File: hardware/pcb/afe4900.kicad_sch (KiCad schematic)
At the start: 19 parts, among them U15 TPS61240YFFR, U16 SFH 7072, U6 AFE4900YZR

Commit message: Fix the review's datasheet errors without changing respiration or the GDTs.
Replace the MCP73831 with a BQ25170 so a flat cell still charges from USB, add the missing series protection and ESP32/CP2102 passives, and withdraw the claim that respiration still works with 51 kΩ in the loop.

Co-authored-by: Riyu-D1 <Riyu-D1@users.noreply.github.com>
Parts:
- R43, R45: value 10M -> 5.11M
- R44, R46: value 10M -> 100k
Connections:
- net +3V3: no longer R43.1, R45.1
- net AFE_INM: no longer R46.1
- net AFE_INP: no longer R44.1
- net AFE_N_AC: now also R46.1; no longer C57.1
- net AFE_P_AC: now also R44.1; no longer C56.1
- net GND: no longer R44.2, R46.2
- new net AFE_N_SER: C57.1, R46.2
- new net AFE_P_SER: C56.1, R44.2
- new net RLDOUT: R43.1, R45.1
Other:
- note added: "R44/R46 are 100k on the TPD side. R43/R45 bias from ADS RLDOUT, not a second RLD amp."
- note removed: "R9 holds RESETZ down until the expander drives it. R10 holds CLK low. AFE RLD_OUT is open."

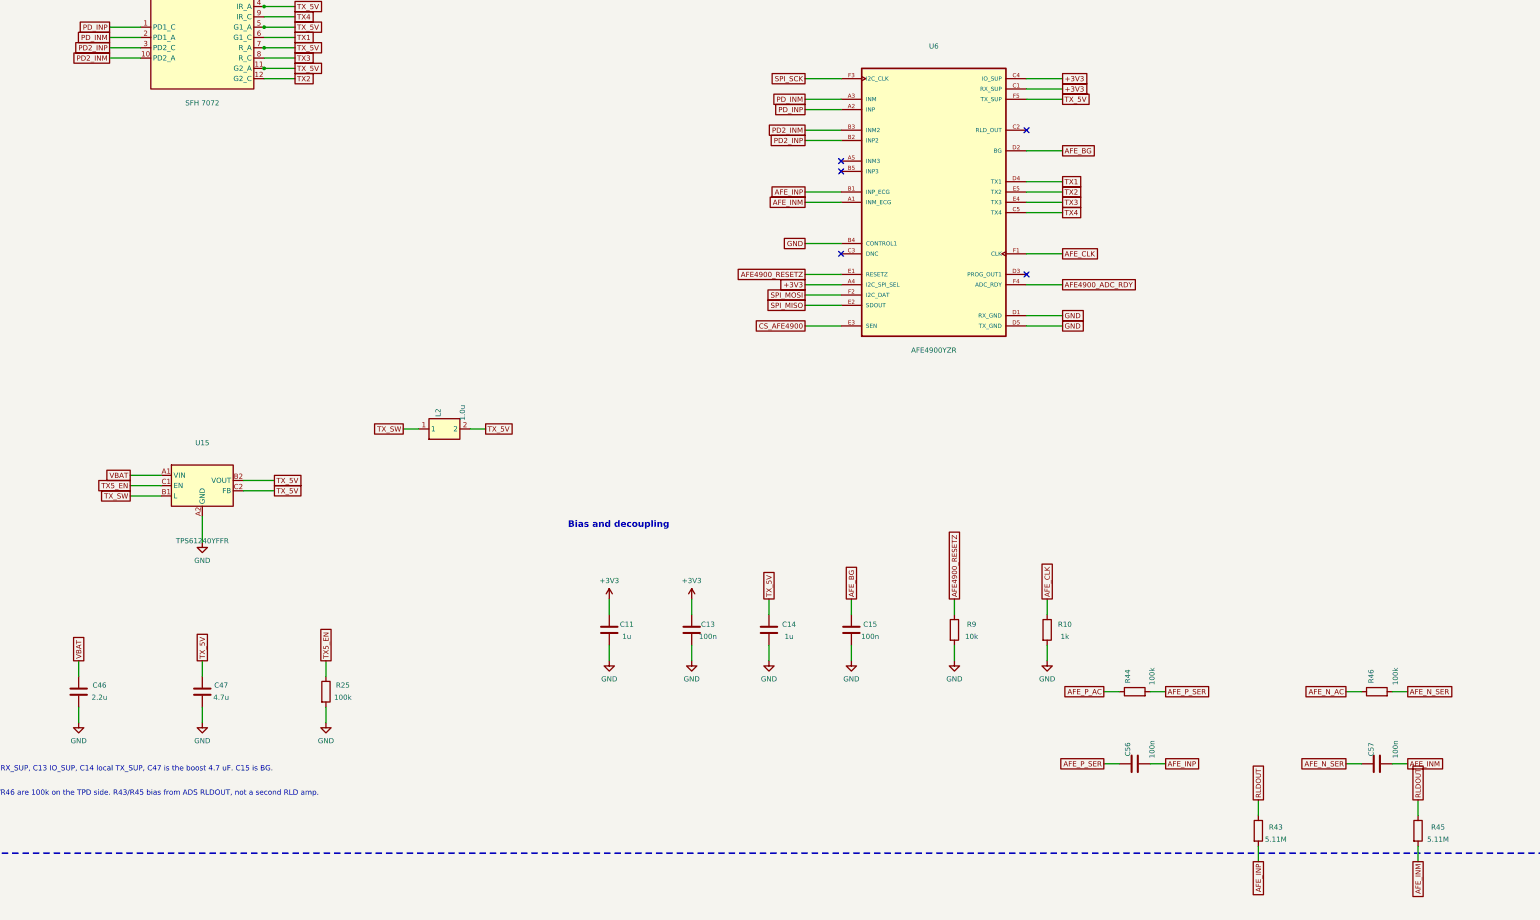
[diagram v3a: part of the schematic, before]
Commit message: Prepare hw_v1 for prefab review without claiming the route is finished.
Add the gauge TDFN, USB ESD, sense links, test access, and JLC BOM fields, and keep the partial Freerouting result with the remaining open nets listed.

Co-authored-by: Riyu-D1 <Riyu-D1@users.noreply.github.com>
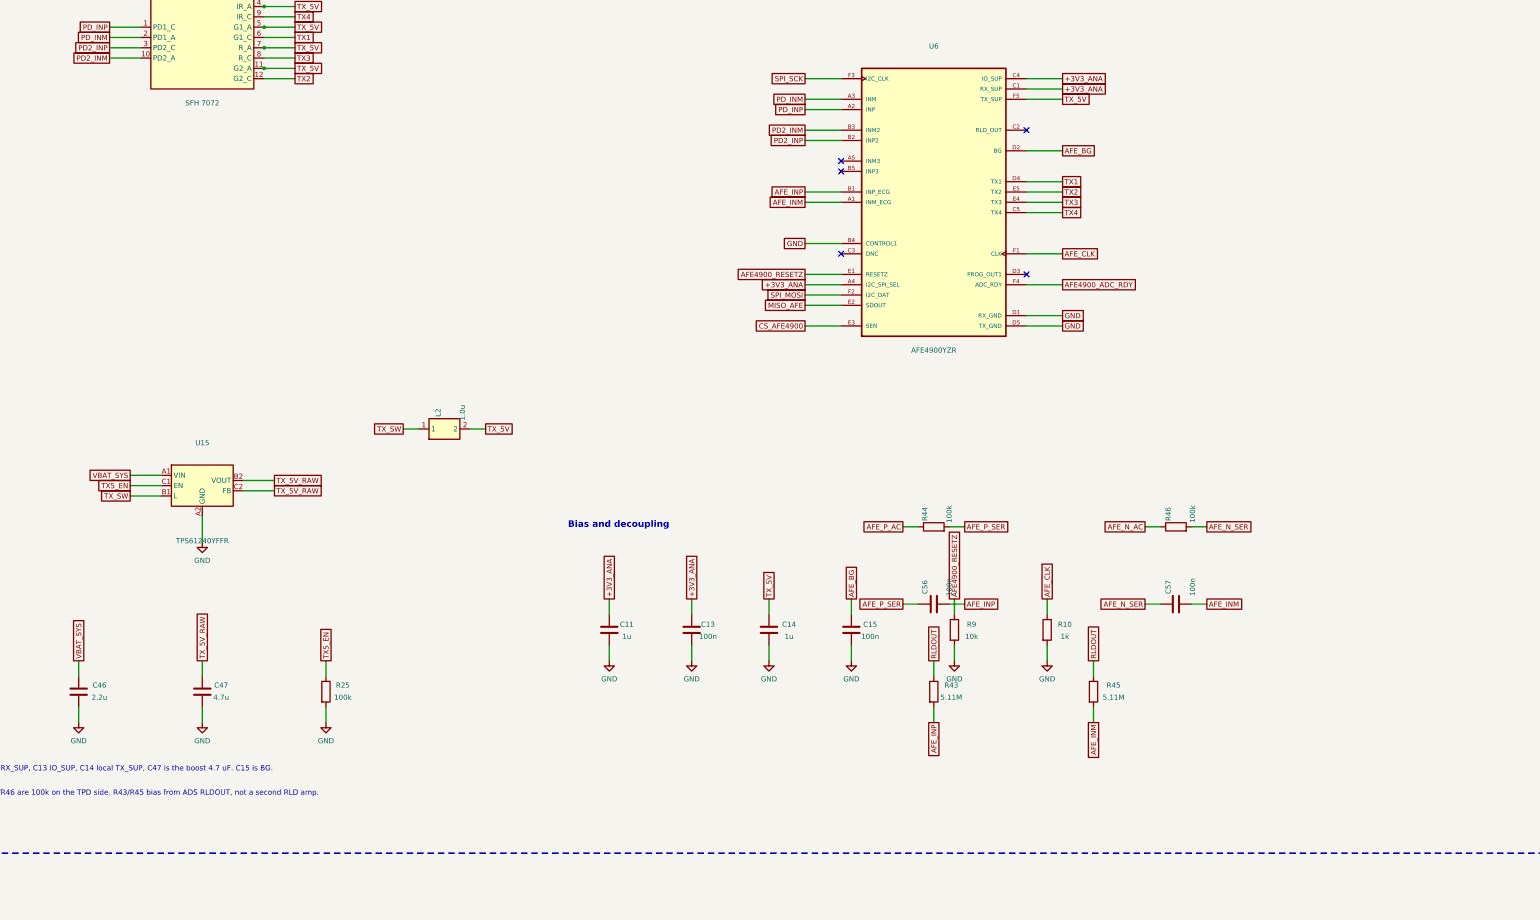
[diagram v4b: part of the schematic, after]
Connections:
- net TX_5V: no longer C47.1, U15.B2 (VOUT), U15.C2 (FB)
- net +3V3 renamed +3V3_ANA
- net SPI_MISO renamed MISO_AFE
- net VBAT renamed VBAT_SYS
- new net TX_5V_RAW: C47.1, U15.B2 (VOUT), U15.C2 (FB)
